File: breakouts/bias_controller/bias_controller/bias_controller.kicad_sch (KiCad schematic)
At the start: 0 parts

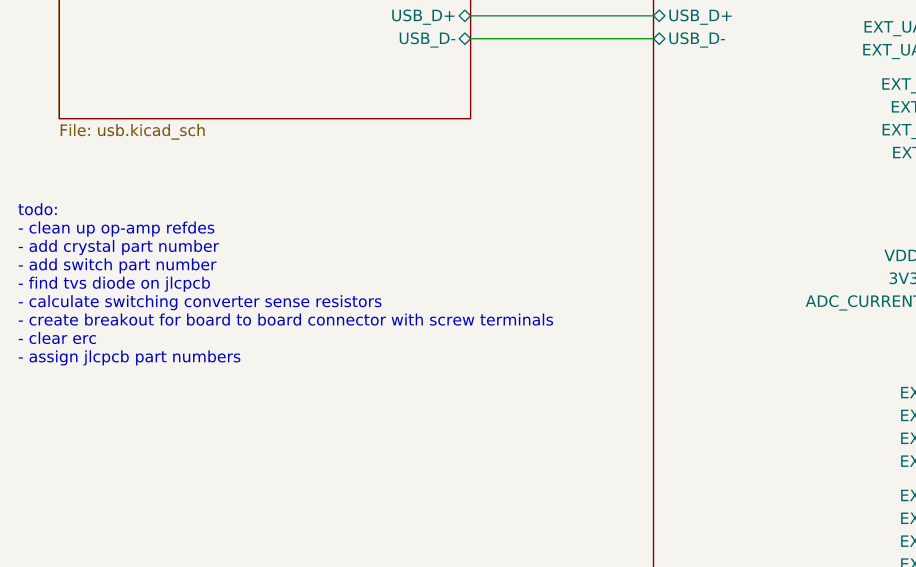
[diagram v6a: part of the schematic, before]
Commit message: schematic and footprint assignment cleanup
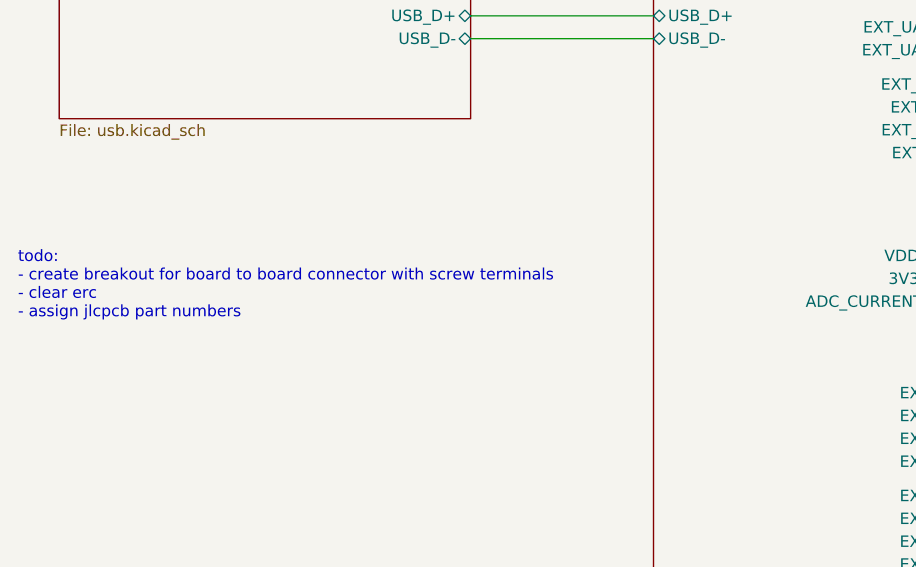
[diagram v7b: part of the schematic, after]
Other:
- note added: "todo: - create breakout for board to board connector with screw terminals - clear erc - assign jlcpcb part numbers"
- note removed: "todo: - clean up op-amp refdes - add crystal part number - add switch part number - find tvs diode on jlcpcb - calculate switching converter sense resistors - create breakout for board to board connector with screw terminals - clear erc - assign jlcpcb part numbers"
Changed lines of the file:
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@@
 		)
 	)
-	(text "todo:\n- clean up op-amp refdes\n- add crystal part number\n- add switch part number\n- find tvs diode on jlcpcb\n- calculate switching converter sense resistors\n- create breakout for board to board connector with screw terminals\n- clear erc\n- assign jlcpcb part numbers"
+	(text "todo:\n- create breakout for board to board connector with screw terminals\n- clear erc\n- assign jlcpcb part numbers"
 		(exclude_from_sim no)
 		(at 15.748 99.822 0)
